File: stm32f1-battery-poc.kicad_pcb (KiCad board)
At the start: 4 copper layers, 92.5 x 85 mm, 153 parts, among them J1 Conn_01x02, J10 Conn_02x03_Odd_Even, J11 Conn_02x03_Odd_Even, J12 Conn_02x03_Odd_Even, J2 Conn_02x02_Odd_Even, J3 Conn_02x03_Odd_Even, J4 Conn_02x07_Odd_Even, J5 Conn_02x02_Odd_Even, J6 Conn_02x02_Odd_Even, J7 Conn_02x03_Odd_Even, J8 Conn_01x02, J9 Conn_01x04_Pin, M1 Stepper_Motor_bipolar, M2 Motor_3_Phases, Q1 Q_NMOS, Q2 Q_NMOS, SW1 SW_Push, SW2 SW_Push, SW3 SW_Push, SW4 SW_SPST, U1 LM78M05, U10 DRV8311H, U2 HT753-1, U3 SN65HVD230, U4 QRE1113GR, U5 QRE1113GR, U6 QRE1113GR, U7 DRV8424RGER, U8 STM32F103C8Tx, U9 BQ77905, Y1 8M

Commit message: pcb: add CAN routing
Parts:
- moved JP4 1.60 mm to (147.5, 104.8)
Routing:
- net /CAN_RX: track 0.00 -> 52.8 mm, vias 0 -> 2
- net /CAN_TX: track 0.00 -> 48.2 mm, vias 0 -> 2
- net /CANL: track 0.00 -> 12.7 mm
- net /CANH: track 0.00 -> 6.63 mm
- net Net-(JP1-B): track 0.00 -> 4.53 mm
- net Net-(JP2-B): track 0.00 -> 3.68 mm

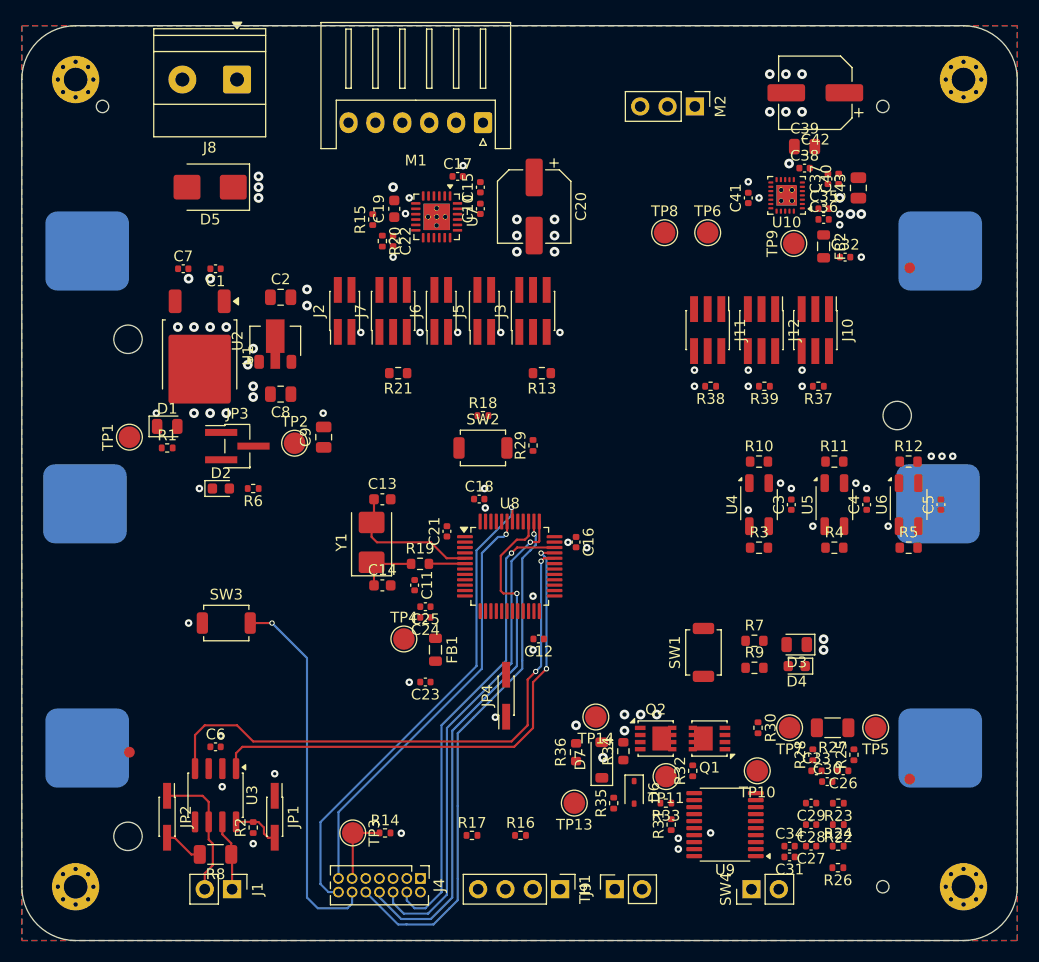
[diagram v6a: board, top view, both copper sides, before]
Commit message: pcb: add DRV8311 routing
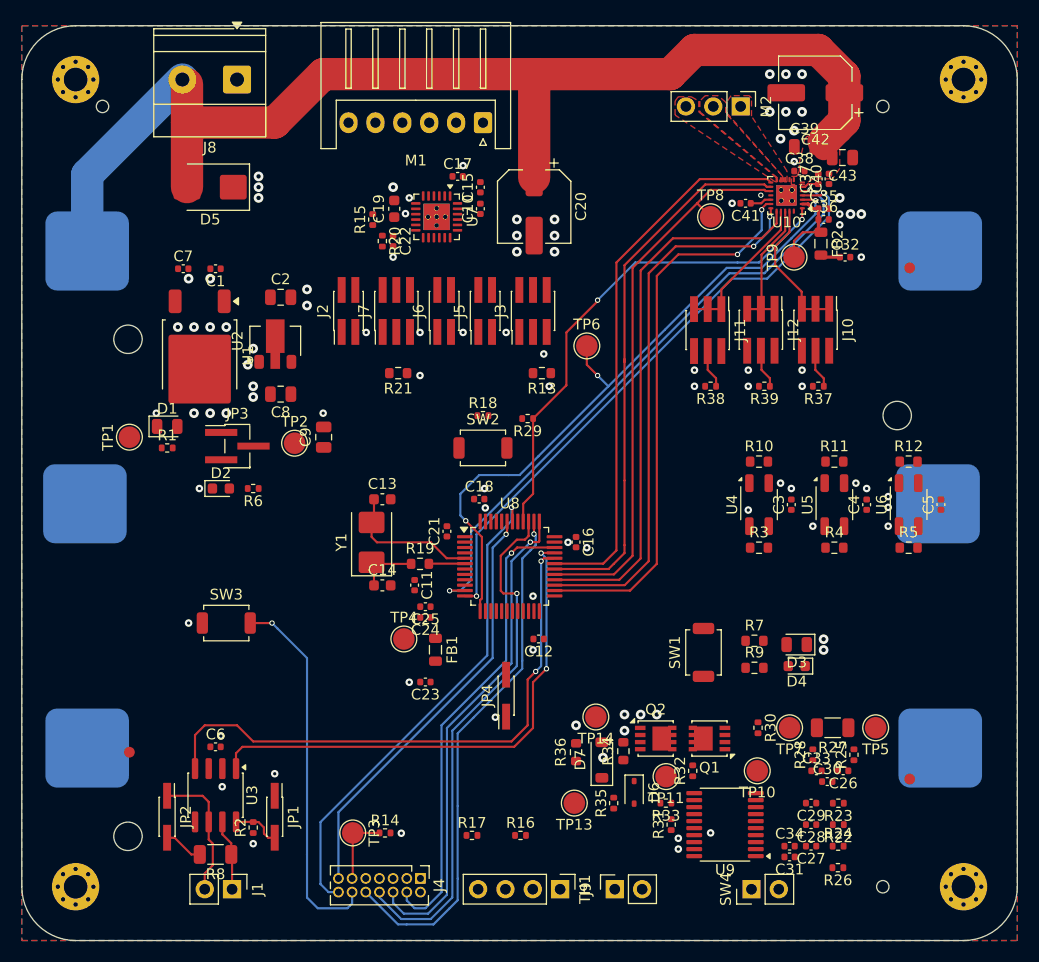
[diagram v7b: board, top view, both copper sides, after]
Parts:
- moved TP6 15.4 mm to (155.0, 72.2)
- moved TP8 4.52 mm to (166.5, 60.2)
- moved M2 4.25 mm to (169.3, 50.0)
- moved C43 3.18 mm to (178.8, 54.8), turned to 180 degrees
- moved R29 2.55 mm to (149.5, 79.0), turned to 180 degrees
- moved TP9 1.27 mm to (174.2, 64.0)
- moved C37 0.90 mm to (176.5, 56.7)
- moved C40 0.90 mm to (177.5, 56.7)
- moved C41 0.56 mm to (169.8, 59.0), turned to 180 degrees
- moved C38 0.55 mm to (174.8, 56.0)
- moved J2 0.35 mm to (132.9, 69.0)
- moved FB2 0.35 mm to (176.8, 62.8)
- moved J7 0.30 mm to (137.3, 69.0)
- moved J6 0.27 mm to (141.7, 69.0)
- moved J5 0.08 mm to (145.6, 69.0)
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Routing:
- net +BATT: track 0.00 -> 111.9 mm
- net /SOC: track 0.00 -> 62.6 mm, vias 0 -> 3
- net /SOA: track 0.00 -> 57.0 mm, vias 0 -> 2
- net /SOB: track 0.00 -> 56.3 mm, vias 0 -> 2
- net /INHA: track 0.00 -> 52.4 mm
- net /INLA: track 0.00 -> 51.8 mm, vias 0 -> 2
- net /INLB: track 0.00 -> 51.4 mm, vias 0 -> 2
- net /INLC: track 0.00 -> 51.2 mm
- net /INHB: track 0.00 -> 50.9 mm
- net /INHC: track 0.00 -> 50.7 mm
- net /~{FAULT}: track 0.00 -> 46.6 mm, vias 0 -> 2
- net /HW interface1/pin: track 0.00 -> 13.9 mm
- net /HW interface/pin: track 0.00 -> 13.2 mm
- net /HW interface2/pin: track 0.00 -> 12.6 mm
- net Net-(U10-CSAREF): track 0.00 -> 8.25 mm
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- added copper zone on F.Cu, net +BATT
- added copper zone on F.Cu, net Net-(U10-OUTA)
- added copper zone on F.Cu, net Net-(U10-OUTB)
- added copper zone on F.Cu, net Net-(U10-OUTC)

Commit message: pcb: add BQ77905 routing
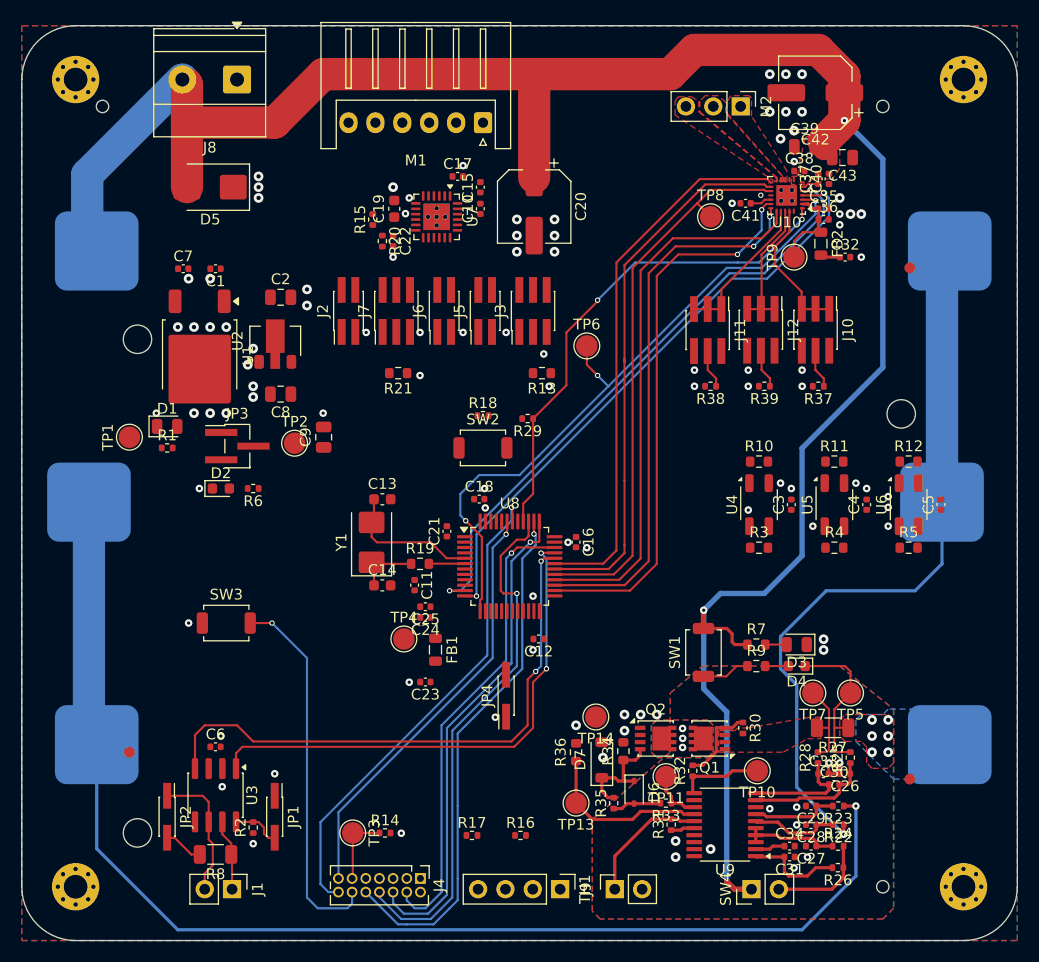
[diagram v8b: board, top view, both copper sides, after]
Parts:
- moved TP5 3.99 mm to (179.5, 104.5)
- moved TP7 3.89 mm to (176.0, 104.5)
- moved R30 1.41 mm to (169.5, 107.8)
- moved BT3 0.94 mm to (149.1, 109.5)
- moved BT1 0.88 mm to (149.1, 63.6)
- moved C30 0.70 mm to (178.0, 113.0)
- moved C33 0.70 mm to (177.0, 112.0)
- moved R28 0.55 mm to (176.5, 110.5)
- moved R25 0.43 mm to (179.5, 110.5)
- moved BT2 0.40 mm to (148.4, 86.6)
- moved R7 0.39 mm to (170.8, 100.0)
- moved C26 0.32 mm to (179.0, 112.0)
- moved R23 0.26 mm to (178.4, 115.0)
- moved C29 0.26 mm to (175.8, 115.0)
- moved R9 0.24 mm to (170.8, 102.0)
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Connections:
- U9 pad 17: GND -> BGND
- U9 pad 18: GND -> BGND
- U9 pad 19: GND -> BGND
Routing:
- net Net-(BT2--): track 1.17 -> 116.9 mm, vias 0 -> 1
- net +BATT: track 111.9 -> 203.7 mm, vias 0 -> 2
- net Net-(BT1--): track 0.00 -> 68.7 mm, vias 0 -> 1
- net BGND: track 0.00 -> 18.2 mm, vias 0 -> 16
- net Net-(U9-LD): track 0.00 -> 15.9 mm
- net Net-(U9-TS): track 0.00 -> 12.0 mm
- net Net-(U9-SRP): track 0.00 -> 11.7 mm
- net Net-(U9-SRN): track 0.00 -> 10.3 mm
- net Net-(D6-K): track 0.00 -> 10.0 mm
- net Net-(SW4-B): track 0.00 -> 9.38 mm
- net Net-(U9-VC3): track 0.00 -> 9.10 mm
- net Net-(U9-VDD): track 0.00 -> 9.01 mm
- net Net-(U9-VC2): track 0.00 -> 8.20 mm
- net Net-(Q1-S-Pad1): track 0.00 -> 8.11 mm
- net Net-(U9-VC1): track 0.00 -> 8.09 mm
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- added copper zone on B.Cu, net BGND
- added copper zone on F.Cu, net BGND
- added copper zone on In1.Cu, net BGND
- added copper zone on In2.Cu, net BGND
- added copper zone on B.Cu, net Net-(Q1-D)
- added copper zone on F.Cu, net Net-(Q1-D)
- added copper zone on F.Cu, net Net-(Q1-S-Pad1)
